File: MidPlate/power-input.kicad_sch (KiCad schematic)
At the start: 8 parts, among them J1 XT60, J2 XT60, Q1 FDD86250-F085, Q2 FDD86250-F085

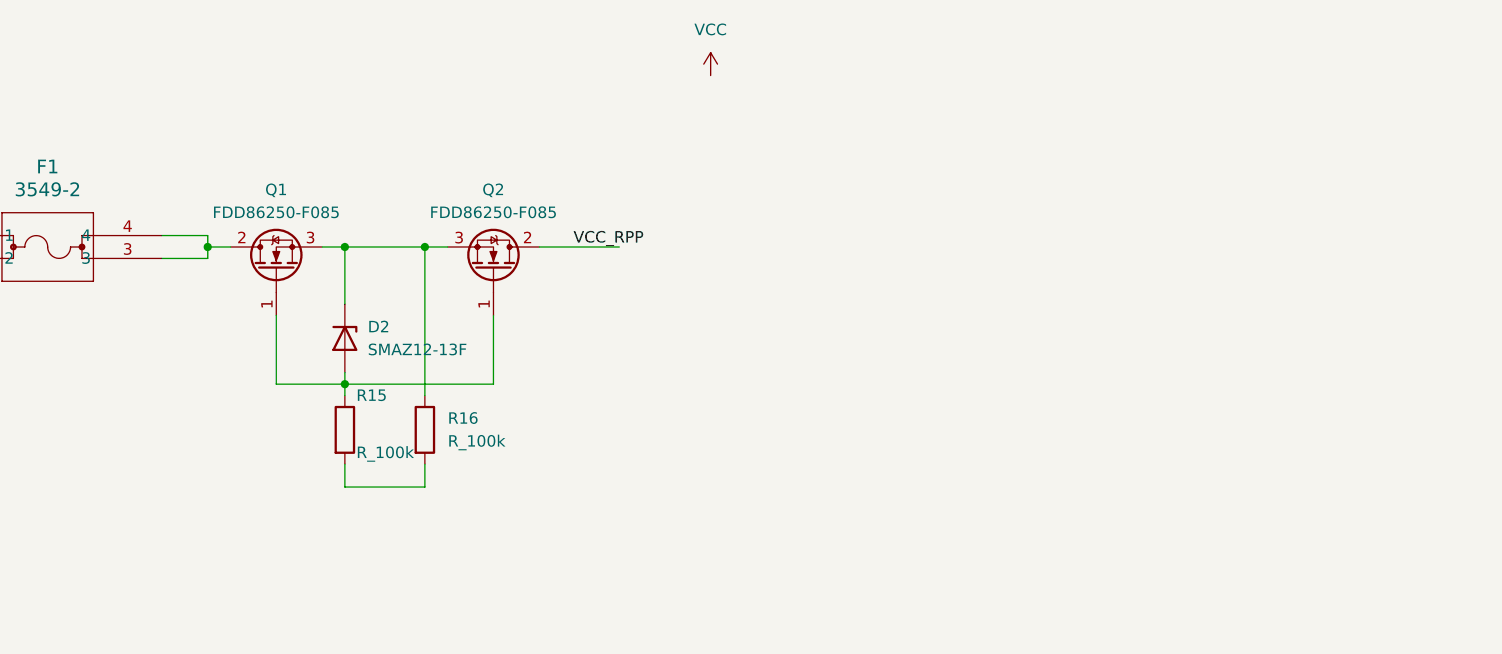
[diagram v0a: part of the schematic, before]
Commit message: added switch and fuse
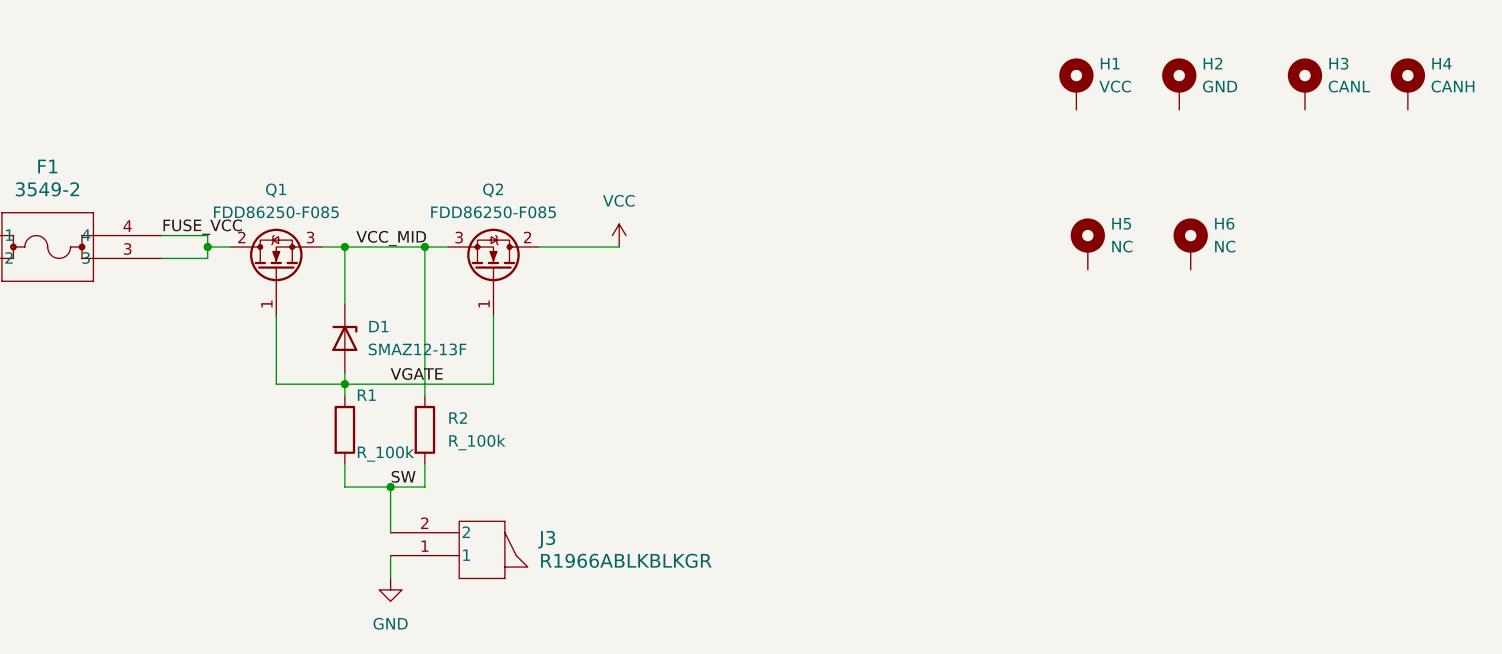
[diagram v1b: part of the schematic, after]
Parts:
- added H1: VCC, bots:MountingHole_2.7mm_M2.5_DIN965_Pad, symbol Mechanical:MountingHole_Pad
- added H2: GND, bots:MountingHole_2.7mm_M2.5_DIN965_Pad, symbol Mechanical:MountingHole_Pad
- added H3: CANL, bots:MountingHole_2.7mm_M2.5_DIN965_Pad, symbol Mechanical:MountingHole_Pad
- added H4: CANH, bots:MountingHole_2.7mm_M2.5_DIN965_Pad, symbol Mechanical:MountingHole_Pad
- added H5, H6: NC, bots:MountingHole_2.7mm_M2.5_DIN965_Pad, symbol Mechanical:MountingHole_Pad
- added J3: R1966ABLKBLKGR, bots:SW_R1966ABLKBLKGR, symbol bots:R1966ABLKBLKGR
- F1: footprint FUSE_3549-2_KEY -> bots:FUSE_3549-2_KEY
- renumbered D2 to D1, R15 to R1, R16 to R2
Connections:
- net VCC_RPP is gone; now on net VCC: Q2.2 (D)
- net GND: now also J3.1
- net VGATE: now reaches D1.2 (A), Q1.1 (G), Q2.1 (G), R1.1
- net VCC_MID: now reaches D1.1 (K), Q1.3 (S), Q2.3 (S), R2.1
- net FUSE_VCC: now reaches F1.3, F1.4, Q1.2 (D)
- net SW: now reaches R1.2, R2.2
- net SW: now also J3.2

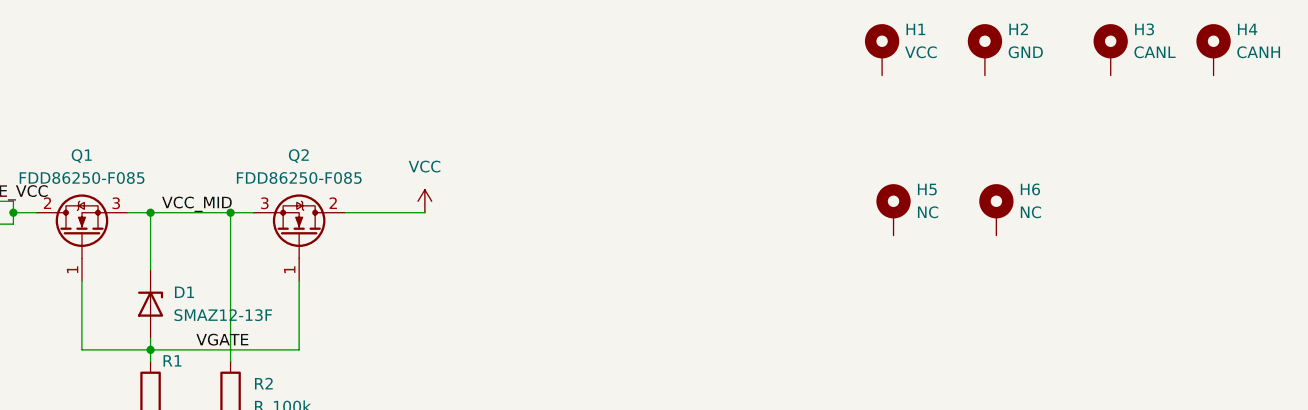
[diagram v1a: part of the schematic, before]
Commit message: powerboard HV powerpillars + midplate
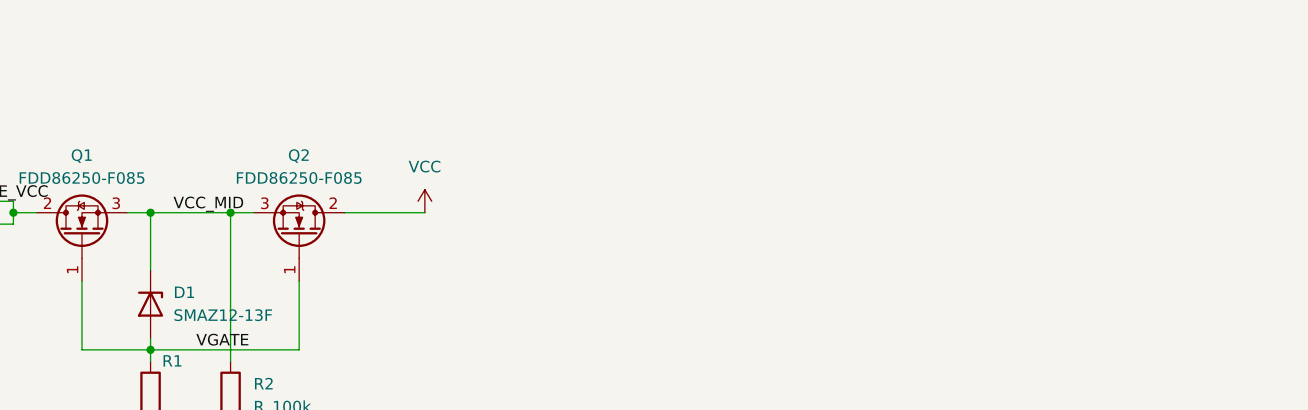
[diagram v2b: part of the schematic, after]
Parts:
- removed H1: VCC, bots:MountingHole_2.7mm_M2.5_DIN965_Pad, symbol Mechanical:MountingHole_Pad
- removed H2: GND, bots:MountingHole_2.7mm_M2.5_DIN965_Pad, symbol Mechanical:MountingHole_Pad
- removed H3: CANL, bots:MountingHole_2.7mm_M2.5_DIN965_Pad, symbol Mechanical:MountingHole_Pad
- removed H4: CANH, bots:MountingHole_2.7mm_M2.5_DIN965_Pad, symbol Mechanical:MountingHole_Pad
- removed H5, H6: NC, bots:MountingHole_2.7mm_M2.5_DIN965_Pad, symbol Mechanical:MountingHole_Pad

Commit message: update to midplate
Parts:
- removed D1: SMAZ12-13F, bots:D_SMB, symbol bots:D_ZENER_3SMBJ5929B-TP
- removed F1: 3549-2, bots:FUSE_3549-2_KEY, symbol bots:3549-2
- removed J3: R1966ABLKBLKGR, bots:SW_R1966ABLKBLKGR, symbol bots:R1966ABLKBLKGR
- removed Q1, Q2: FDD86250-F085, bots:DPAK-3_ONS, symbol bots:FDD86250-F085
- added D1: SMAZ12-13F, bots:D_SMB, symbol bots:D_ZENER_SMAZ12-13F
- added F1: 3568, Fuse:Fuseholder_Blade_Mini_Keystone_3568, symbol bots:3568
- added J3: JS202011JAQN, bots:JS202011JAQN, symbol bots:JS202011JAQN
- added Q1, Q2: IPD85P04P4-07, bots:DPAK-3_ONS, symbol bots:IPD85P04P4-07
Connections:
- net FUSE_VCC: now also F1.2, Q1.2 (D)
- net GND: now also J3.1, J3.2 (2-_C)
- net SW: now also J3.3
- net VBAT: now also F1.1
- net VCC: now also Q2.2 (D)
- net VCC_MID: now also D1.1 (K), Q1.3 (S), Q2.3 (S)
- net VGATE: now also D1.2 (A), Q1.1 (G), Q2.1 (G)
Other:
- moved on the sheet: J1, J2

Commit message: midplate mods
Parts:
- removed J3: JS202011JAQN, bots:JS202011JAQN, symbol bots:JS202011JAQN
- removed Q1, Q2: IPD85P04P4-07, bots:DPAK-3_ONS, symbol bots:IPD85P04P4-07
- added J3: R1966ABLKBLKGR, bots:SW_R1966ABLKBLKGR, symbol bots:R1966ABLKBLKGR
- added J6: EG1206, bots:SW_EG1206, symbol bots:SW_EG1206
- added Q1, Q2, Q3: MCU60P04-TP, bots:DPAK-3_ONS, symbol bots:MCU60P04-TP
- added R15, R16: R_100k, bots:R_0603_1608Metric, symbol bots:R_100k
- F1: footprint Fuse:Fuseholder_Blade_Mini_Keystone_3568 -> bots:Fuseholder_Blade_Mini_Keystone_3568
- J1, J2: footprint bots:Amass_XT60PW-M -> bots:XT60_12-14AWG_POWER
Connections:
- net FUSE_VCC: now also Q1.2 (D)
- net GND: now also J3.1, J6.3
- net SW: now also J6.2 (2-_C)
- net VCC: now also Q3.2 (D)
- net VCC_MID: now also Q1.3 (S), Q2.3 (S)
- net VGATE: now also Q1.1 (G), Q2.1 (G)
- new net SW2: J3.2, R15.2, R16.2
- new net VCOM: Q2.2 (D), Q3.3 (S), R15.1
- new net VGATE2: Q3.1 (G), R16.1
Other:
- moved on the sheet: D1, F1, J1, J2, R1, R2

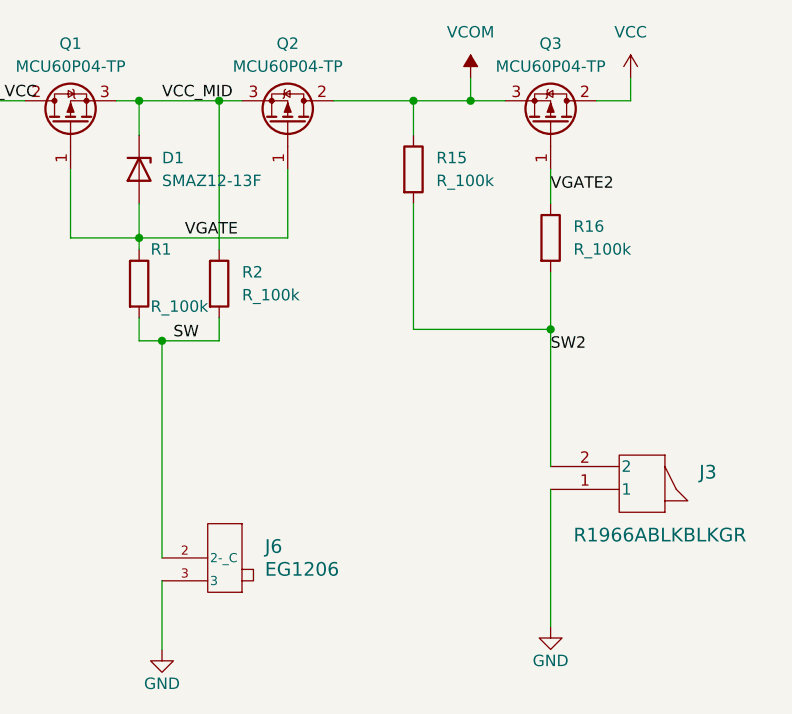
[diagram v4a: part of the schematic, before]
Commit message: midplate updates
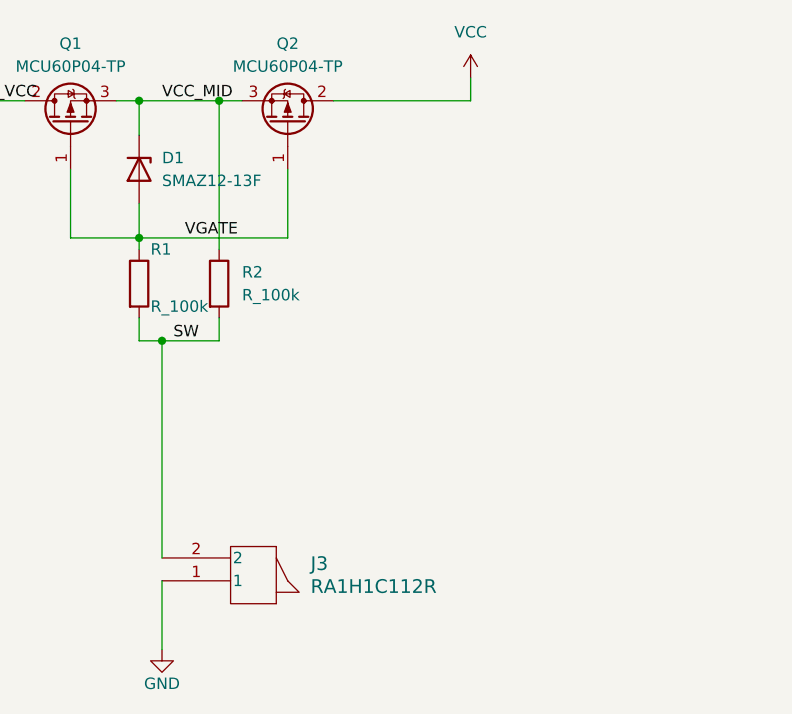
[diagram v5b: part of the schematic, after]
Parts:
- removed J3: R1966ABLKBLKGR, bots:SW_R1966ABLKBLKGR, symbol bots:R1966ABLKBLKGR
- removed J6: EG1206, bots:SW_EG1206, symbol bots:SW_EG1206
- removed Q3: MCU60P04-TP, bots:DPAK-3_ONS, symbol bots:MCU60P04-TP
- removed R15, R16: R_100k, bots:R_0603_1608Metric, symbol bots:R_100k
- added J3: RA1H1C112R, bots:SW_RA1H1C112R, symbol bots:RA1H1C112R
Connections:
- net VCOM is gone; now on net VCC: Q2.2 (D)
- net GND: now also J3.1
- net SW: now also J3.2

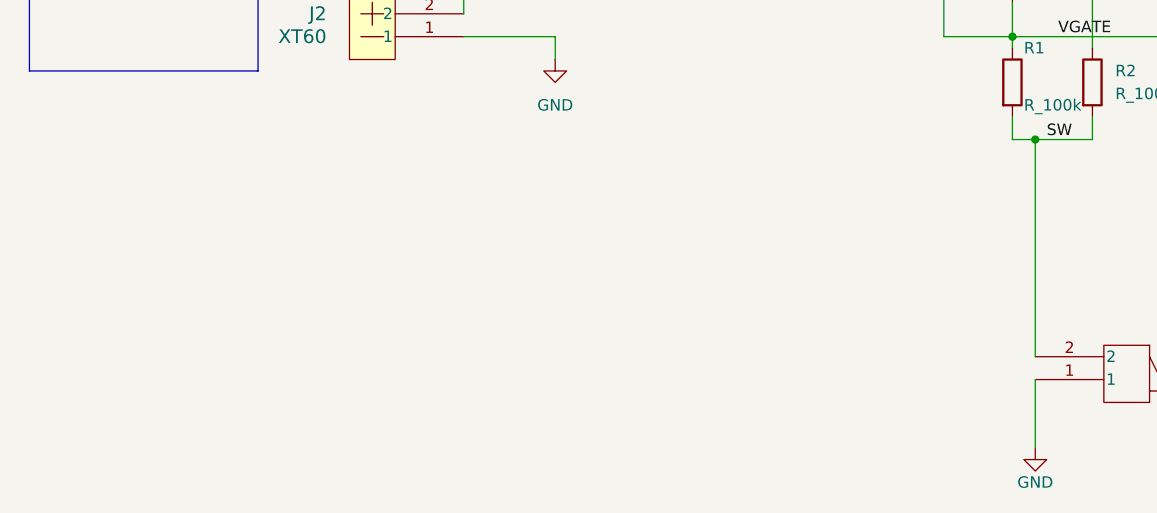
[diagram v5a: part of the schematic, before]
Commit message: midplate 5V buck converter
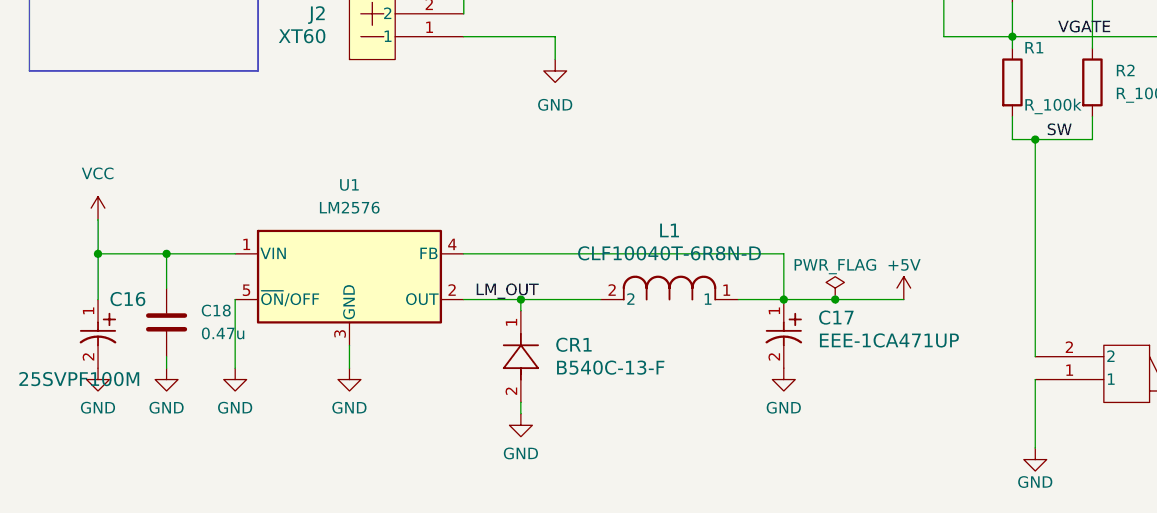
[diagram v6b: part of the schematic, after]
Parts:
- added C16: 25SVPF100M, bots:PCAP_SVP_E7_PAN, symbol bots:25SVPF100M
- added C17: EEE-1CA471UP, bots:CAP_EEE_F_PAN, symbol bots:EEE-1CA471UP
- added C18: 0.47u, Capacitor_SMD:C_1206_3216Metric, symbol bots:C_0.47u
- added CR1: B540C-13-F, bots:SMC_DIO, symbol bots:B540C-13-F
- added L1: CLF10040T-6R8N-D, bots:IND_10040_TDK, symbol bots:CLF10040T-6R8N-D
- added U1: LM2576, bots:TO-263-5_TabPin3_LM2576, symbol bots:LM2576
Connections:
- net GND: now also C16.2, C17.2, C18.2, CR1.2, U1.3 (GND), U1.5 (~{ON}/OFF)
- net VCC: now also C16.1, C18.1, U1.1 (VIN)
- new net +5V: C17.1, L1.1, U1.4 (FB)
- new net LM_OUT: CR1.1, L1.2, U1.2 (OUT)

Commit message: midplate v1 ready for review
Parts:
- removed L1: CLF10040T-6R8N-D, bots:IND_10040_TDK, symbol bots:CLF10040T-6R8N-D
- added L1: SRP1050WA-101M, bots:SRP1050WA-101M, symbol bots:SRP1050WA-101M
- C18: footprint Capacitor_SMD:C_1206_3216Metric -> bots:C_1206_3216Metric
- D1: footprint bots:D_SMB -> bots:D_SMA
- renumbered CR1 to D2
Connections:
- net +5V: now also L1.1
- net LM_OUT: now also L1.2
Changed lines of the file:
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@@
   (symbol (lib_id "bots:B540C-13-F") (at 73.66 86.36 90) (unit 1)
     (in_bom yes) (on_board yes) (dnp no) (fields_autoplaced)
-    (property "Reference" "CR1" (at 77.47 80.01 90)
+    (property "Reference" "D2" (at 77.47 80.01 90)
       (effects (font (size 1.524 1.524)) (justify right))
     )
@@
       (project "midplate"
         (path "/69058343-dac8-421b-a3f6-e069eb1ba8ae/ab54f000-c596-4ae0-81be-92723dd47fdf"
-          (reference "CR1") (unit 1)
+          (reference "D2") (unit 1)
         )
       )
@@
       (effects (font (size 1.27 1.27)) (justify left))
     )
-    (property "Footprint" "bots:D_SMB" (at 128.27 38.1 0)
+    (property "Footprint" "bots:D_SMA" (at 128.27 38.1 0)
       (effects (font (size 1.27 1.27)) hide)
     )
@@
       (effects (font (size 1.27 1.27)) (justify left))
     )
-    (property "Footprint" "Capacitor_SMD:C_1206_3216Metric" (at 35.2552 81.28 0)
+    (property "Footprint" "bots:C_1206_3216Metric" (at 35.2552 81.28 0)
       (effects (font (size 1.27 1.27)) hide)
     )
@@
         (path "/69058343-dac8-421b-a3f6-e069eb1ba8ae/ab54f000-c596-4ae0-81be-92723dd47fdf"
           (reference "Q1") (unit 1)
+        )
+      )
+    )
+  )
+  (symbol (lib_id "bots:SRP1050WA-101M") (at 82.55 74.93 0) (unit 1)
+    (in_bom yes) (on_board yes) (dnp no) (fields_autoplaced)
+    (property "Reference" "L1" (at 90.17 67.31 0)
+      (effects (font (size 1.524 1.524)))
+    )
+    (property "Value" "SRP1050WA-101M" (at 90.17 69.85 0)
+      (effects (font (size 1.524 1.524)))
+    )
+    (property "Footprint" "bots:SRP1050WA-101M" (at 82.55 74.93 0)
+      (effects (font (size 1.27 1.27) italic) hide)
+    )
+    (property "Datasheet" "" (at 82.55 74.93 0)
+      (effects (font (size 1.27 1.27) italic) hide)
+    )
+    (pin "1")
+    (pin "2")
+    (instances
+      (project "midplate"
+        (path "/69058343-dac8-421b-a3f6-e069eb1ba8ae/ab54f000-c596-4ae0-81be-92723dd47fdf"
+          (reference "L1") (unit 1)
         )
       )
@@
         )
       )
-    )
-  )
-  (symbol (lib_id "bots:CLF10040T-6R8N-D") (at 82.55 74.93 0) (unit 1)
-    (in_bom yes) (on_board yes) (dnp no) (fields_autoplaced)
-    (property "Reference" "L1" (at 90.17 67.31 0)
-      (effects (font (size 1.524 1.524)))
-    )
-    (property "Value" "CLF10040T-6R8N-D" (at 90.17 69.85 0)
-      (effects (font (size 1.524 1.524)))
-    )
-    (property "Footprint" "bots:IND_10040_TDK" (at 82.55 74.93 0)
-      (effects (font (size 1.27 1.27) italic) hide)
-    )
-    (property "Datasheet" "CLF10040T-6R8N-D" (at 82.55 74.93 0)
-      (effects (font (size 1.27 1.27) italic) hide)
-    )
-    (pin "1")
-    (pin "2")
-    (instances
-      (project "midplate"
-        (path "/69058343-dac8-421b-a3f6-e069eb1ba8ae/ab54f000-c596-4ae0-81be-92723dd47fdf"
-          (reference "L1") (unit 1)
-        )
-      )
